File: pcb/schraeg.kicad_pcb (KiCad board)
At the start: 2 copper layers, 84.5 x 128.5 mm, 120 parts, among them J1 PJ398SM, J2 PJ398SM, J3 PJ398SM, J4 PJ398SM, J5 PJ398SM, J6 PJ398SM, J7 PJ398SM, J8 POWER, U1 TL074, U2 TL074, U3 V2164, U4 TL074, U5 TL074

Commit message: Consolidate names
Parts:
- G***: footprint Schraeg:silkF -> schraeg:silkF
- G***: footprint Schraeg:copper -> schraeg:copper
- G***: footprint Schraeg:maskF -> schraeg:maskF
- Ref** (x2): footprint Schraeg:Schraeg Panel Graphics Inkscape -> schraeg:schraeg Panel Graphics Inkscape
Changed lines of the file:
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@@
     (add_net "Net-(U3-Pad1)")
   )
-  (module Schraeg:silkF (layer F.Cu)
+  (module schraeg:silkF (layer F.Cu)
     (at 20.25 64.25)
     (fp_text reference G*** (at 0 0) (layer F.SilkS) hide
@@
     )
   )
-  (module Schraeg:copper (layer F.Cu)
+  (module schraeg:copper (layer F.Cu)
     (at 20.25 64.25)
     (fp_text reference G*** (at 0 0) (layer F.SilkS) hide
@@
       (xy -4.456904 59.45542) (xy -4.38831 59.449785) (xy -4.334934 59.450191)) (layer F.Cu) (width 0.01))
   )
-  (module Schraeg:maskF (layer F.Cu)
+  (module schraeg:maskF (layer F.Cu)
     (at 20.25 64.25)
     (fp_text reference G*** (at 0 0) (layer F.SilkS) hide
@@
     )
   )
-  (module "Schraeg:Schraeg Panel Graphics Inkscape" (layer F.Cu)
+  (module "schraeg:schraeg Panel Graphics Inkscape" (layer F.Cu)
     (at 106.9 70.7)
     (fp_text reference Ref** (at 0 0) (layer F.SilkS) hide
@@
     )
   )
-  (module "Schraeg:Schraeg Panel Graphics Inkscape" (layer F.Cu)
+  (module "schraeg:schraeg Panel Graphics Inkscape" (layer F.Cu)
     (at 106.6 25.9)
     (fp_text reference Ref** (at 0 0) (layer F.SilkS) hide

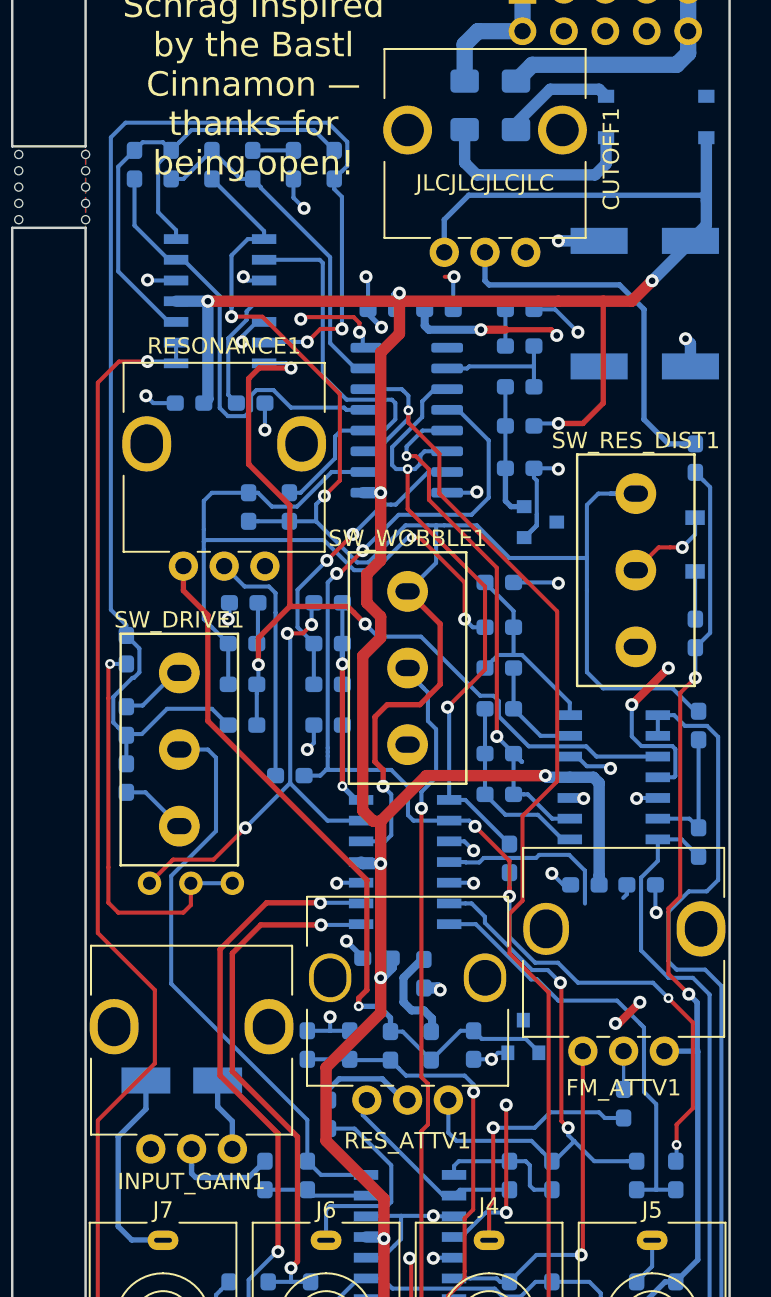
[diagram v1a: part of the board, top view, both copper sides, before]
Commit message: #4 - Added mouser references
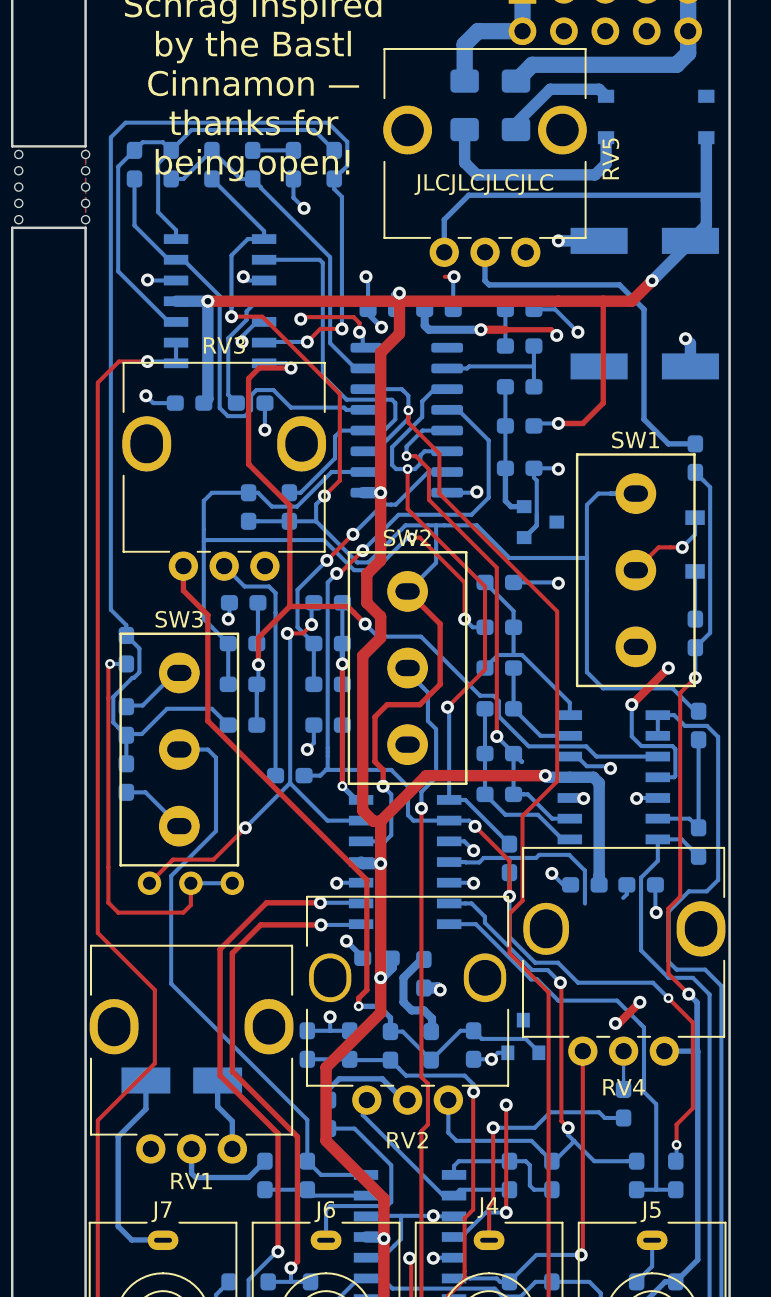
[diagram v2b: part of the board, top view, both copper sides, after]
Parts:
- D1, D2: value D_Small -> 1N4148
- R1, R10, R12, R13, R16, R17, R20, R3, R4, R6, R7, R9: value 100k -> 100K
- R18: value 22k -> 22K
- R19, R22: value 47k -> 47K
- R21: value 10k -> 10K
- R27, R28, R29, R31, R33, R34, R35, R36, R38: value 33k -> 33K
- R41: value 1.5K -> 1K5
- R44, R47: value 6.8K -> 6K8
- R46: value 3.3K -> 3K3
- RV1: renamed from INPUT_GAIN1; value 100k -> 100K
- RV2: renamed from RES_ATTV1; value 100KB -> 100K
- RV3: renamed from RESONANCE1; value 100k -> 100K
- RV4: renamed from FM_ATTV1; value 100KB -> 100K
- RV5: renamed from CUTOFF1; value 100k -> 100KB
- RV6: renamed from RV_SAW_OCTAVE1; value 100k -> 100K
- SW1: renamed from SW_RES_DIST1; value SW_SPDT -> CS12ANW03
- SW2: renamed from SW_WOBBLE1; value SW_SPDT -> CS12ANW03
- SW3: renamed from SW_DRIVE1; value SW_SPDT -> CS12ANW03
- renumbered V_OCT_SCALE1 to RV7, RES_ADJ1 to RV8

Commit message: Tidy up
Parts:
- C1, C12, C7, C8: value 560pF -> 560p
- C10, C11, C13: value 220pF -> 220p
- C16, C17: value 22uF -> 22u
- C2, C4, C5, C6: value 10uF -> 10u
- C3, C9: value 100pF -> 100p
- F1, F2: value Polyfuse -> MF-NSMF050-2
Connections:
- net /Filter Core/AUDIO_IN renamed AUDIO_IN
- net /Filter Core/BP_OUT renamed Net-(C5-Pad1)
- net /Filter Core/FREQ_CV renamed FREQ_CV
- net /Filter Core/HP_OUT renamed Net-(C4-Pad1)
- net /Filter Core/LP_OUT renamed Net-(C6-Pad1)
- net /Filter Core/RES_CV renamed RES_CV
- net /Filter Core/RES_MOD renamed BP_OUT
- net Net-(C13-Pad1) renamed LP_OUT
- net Net-(F1-Pad2) renamed /V-
- net Net-(F2-Pad2) renamed /V+
- net Net-(R28-Pad1) renamed HP_OUT
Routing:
- net Net-(R13-Pad2): track 34.4 -> 36.9 mm

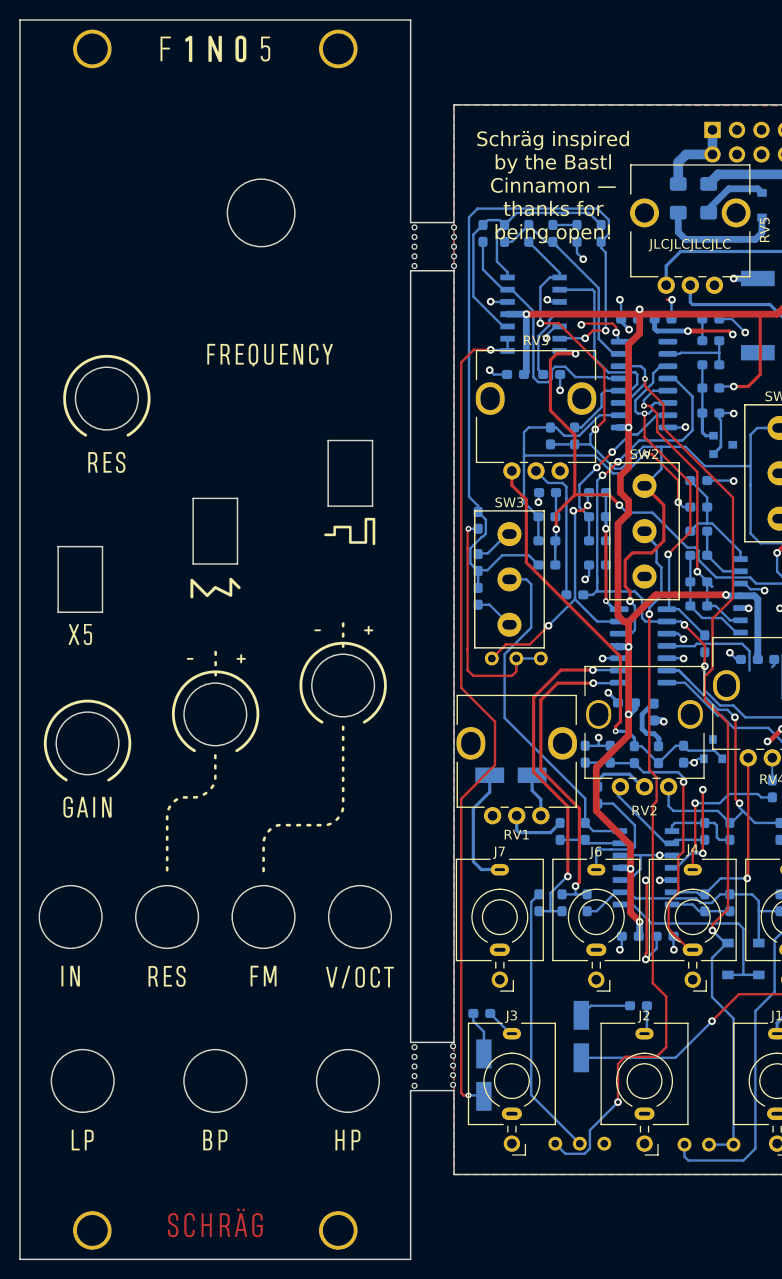
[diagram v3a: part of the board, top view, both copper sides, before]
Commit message: #5 - Removed 0.16V normalization to FM input.
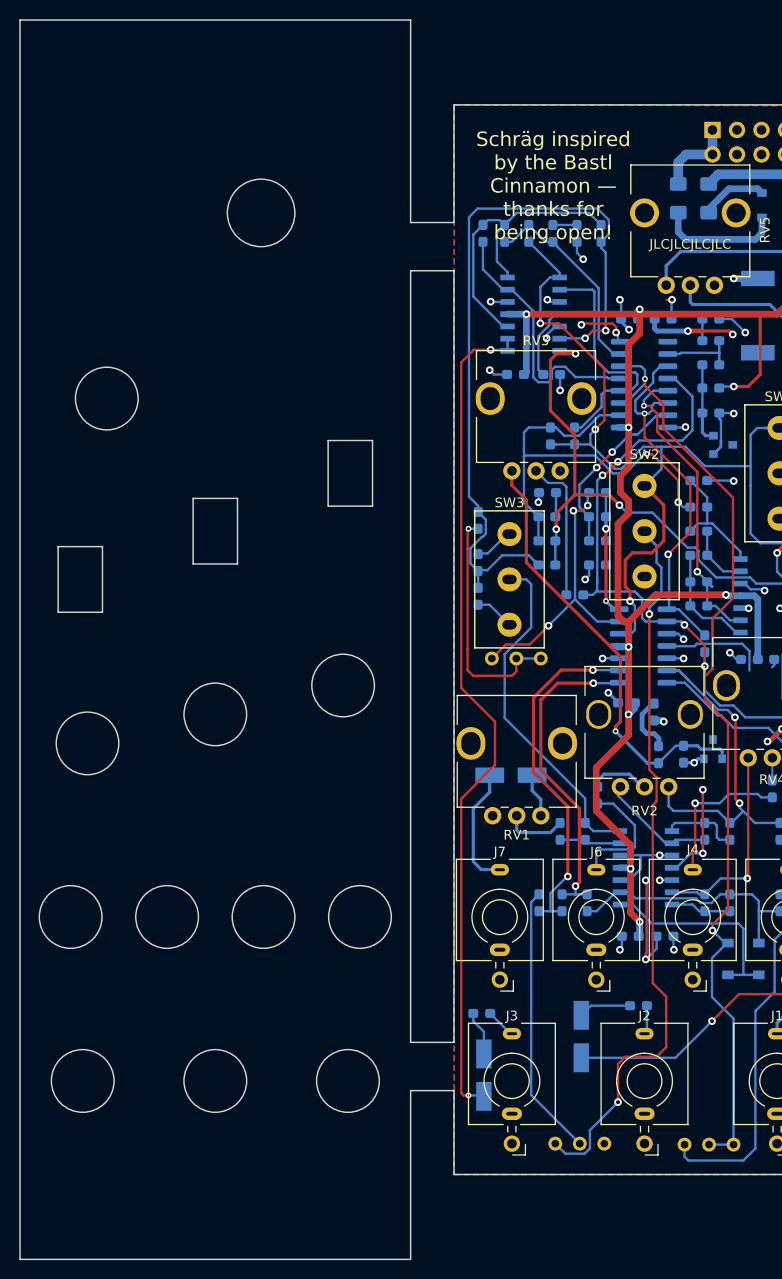
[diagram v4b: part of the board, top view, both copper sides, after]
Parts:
- removed C15: 220n, Capacitor_SMD:C_0603_1608Metric_Pad1.05x0.95mm_HandSolder
- removed G***: LOGO, schraeg:silkF
- removed G***: LOGO, schraeg:copper
- removed G***: LOGO, schraeg:maskF
- removed MOUSEBITE1mm (x4): VAL**, Eurocad:MOUSEBITE1mm
- removed R45: 100K, Resistor_SMD:R_0603_1608Metric_Pad1.05x0.95mm_HandSolder
- removed R46: 3K3, Resistor_SMD:R_0603_1608Metric_Pad1.05x0.95mm_HandSolder
- removed REF** (x4): MountingHole_3.2mm_M3, MountingHole:MountingHole_3.2mm_M3
- removed Ref** (x2): Val**, schraeg:schraeg Panel Graphics Inkscape
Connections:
- J4 pad TN: 0.16V_REF -> GND
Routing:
- net 0.16V_REF: track 30.6 -> 0.00 mm, vias 1 -> 0
- net GND: track 74.9 -> 71.4 mm, vias 33 -> 32

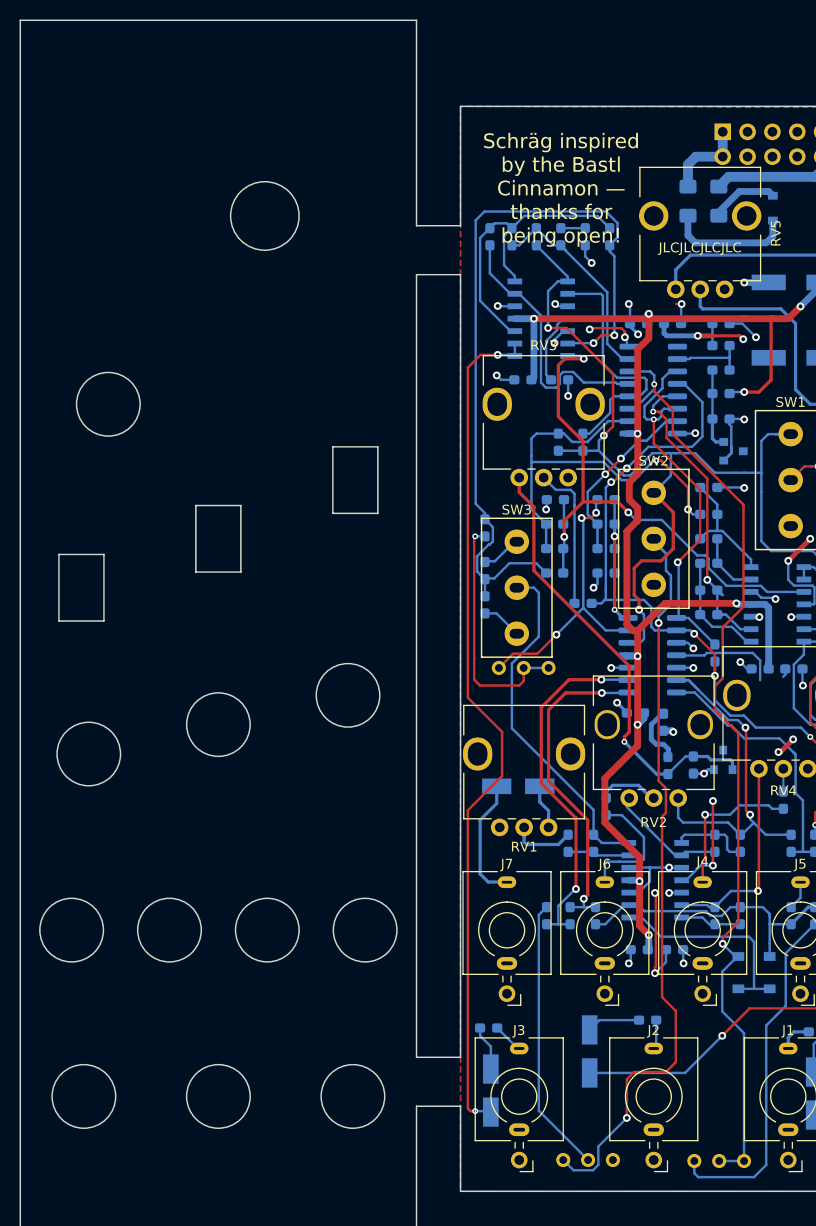
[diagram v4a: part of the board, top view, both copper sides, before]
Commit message: #6 - Replaced the 5V reference with a resistor divider. It should give a voltage of 5.1V.
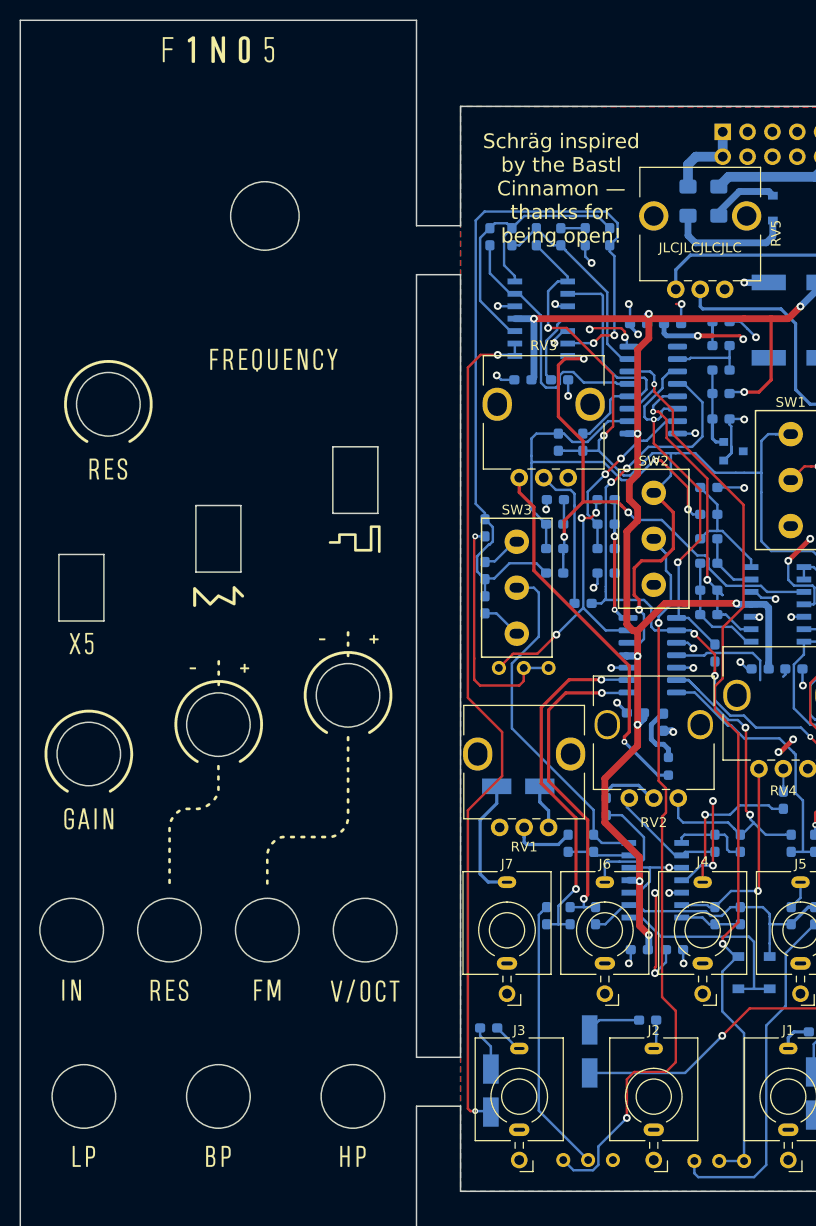
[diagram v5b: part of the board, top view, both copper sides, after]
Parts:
- removed C14: 220n, Capacitor_SMD:C_0603_1608Metric_Pad1.05x0.95mm_HandSolder
- removed D4: LM4040DBZ-5, Package_TO_SOT_SMD:SOT-23
- removed R44: 6K8, Resistor_SMD:R_0603_1608Metric_Pad1.05x0.95mm_HandSolder
- added G***: LOGO, schraeg:silkF, F.Cu at (20.2, 64.2)
- added R8: 56K, Resistor_SMD:R_0603_1608Metric_Pad0.98x0.95mm_HandSolder, B.Cu at (66.2, 76.2)
- moved C1 0.20 mm to (71.6, 30.8)
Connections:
- RV3 pad 3: 5V_REF -> Net-(R8-Pad2)
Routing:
- net 5V_REF: track 46.4 -> 0.00 mm, vias 1 -> 0
- net Net-(R8-Pad2): track 0.00 -> 37.8 mm, vias 0 -> 1
- net GND: track 71.4 -> 69.2 mm, vias 32 -> 31
- net Net-(C1-Pad1): track 2.25 -> 3.40 mm
- net +12V: track 75.0 -> 75.8 mm
